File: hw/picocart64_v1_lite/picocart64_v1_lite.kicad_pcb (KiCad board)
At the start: 2 copper layers, 100 x 60 mm, 12 parts, among them J1 Conn_01x04, J2 Conn_01x07, J3 Conn_01x02, J4 Conn_01x01, J5 Conn_01x01, Q1 BSS84, U1 Pico, U4 N64-Cartridge

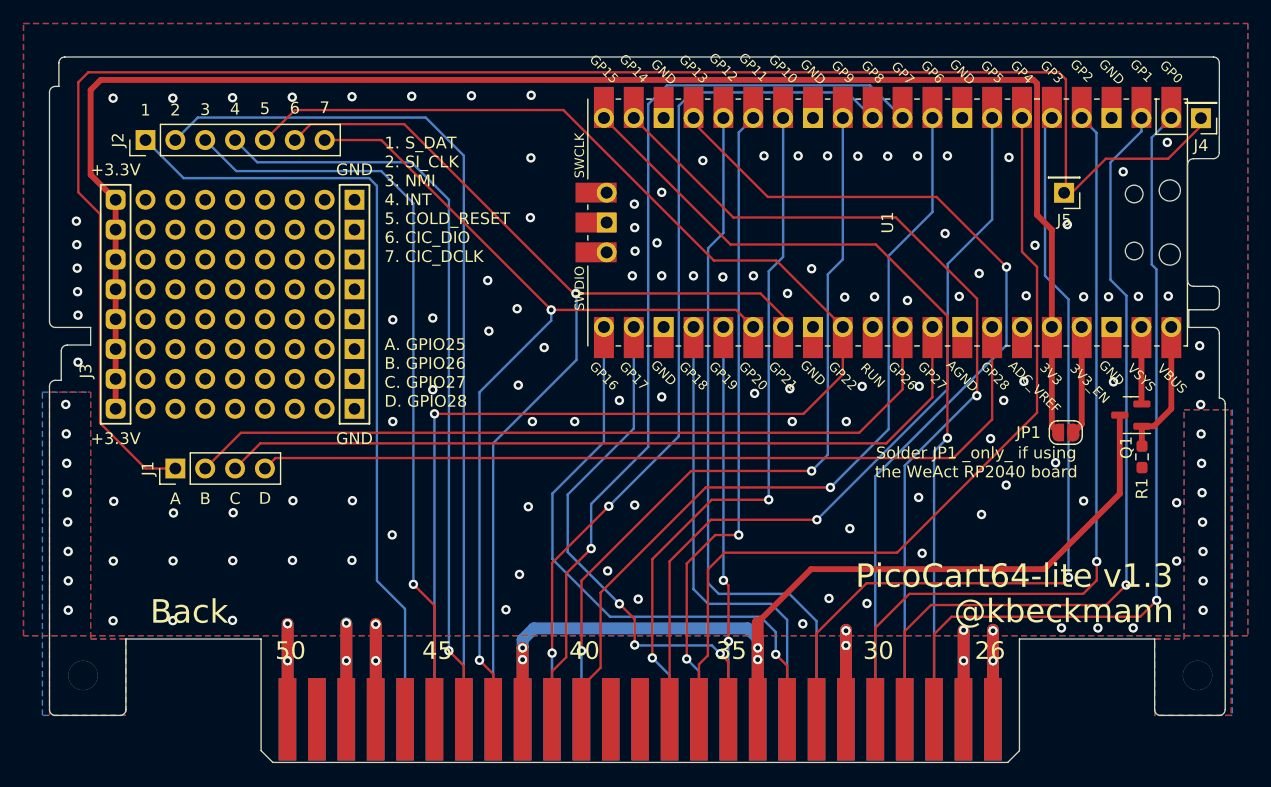
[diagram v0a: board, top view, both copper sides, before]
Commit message: Changes to v1 lite board to allow drop in weact as default instead of pico.
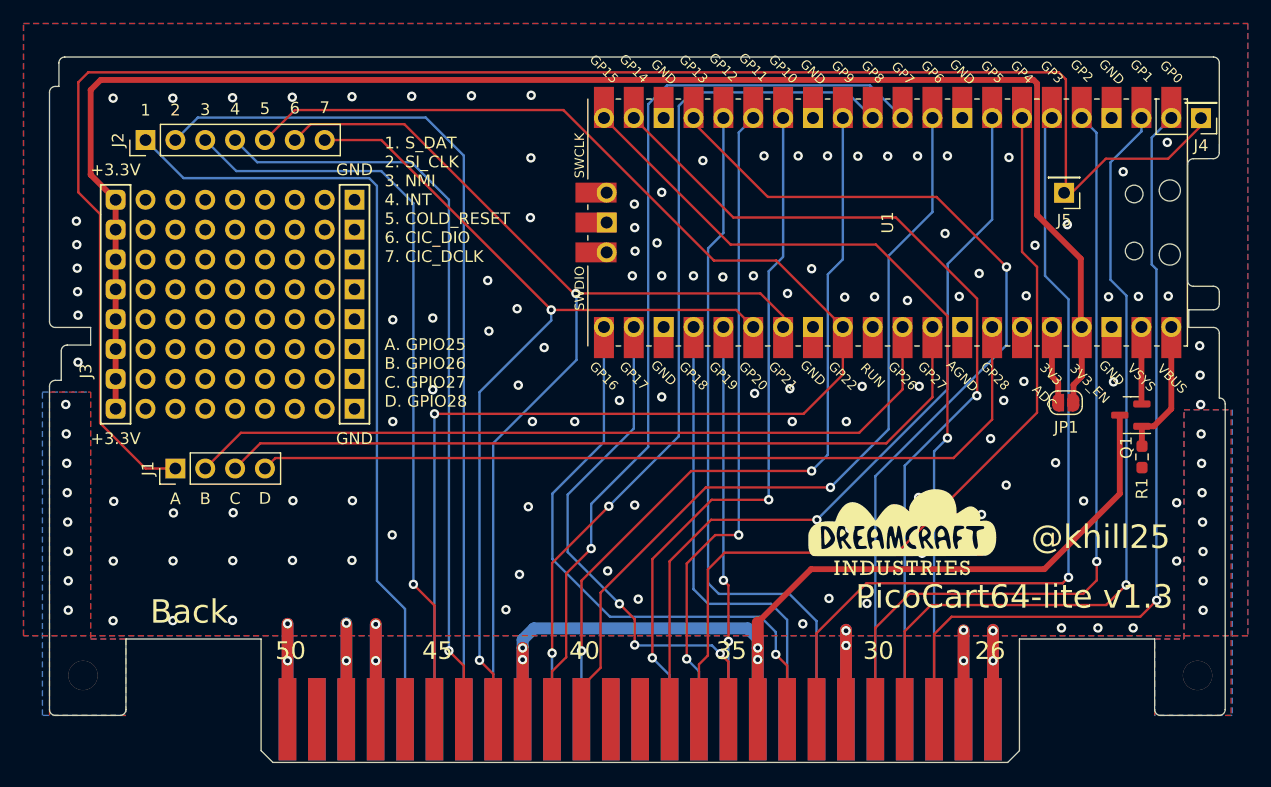
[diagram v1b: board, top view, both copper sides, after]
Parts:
- added G***: LOGO, LOGO, F.Cu at (172.5, 100.8)
- added G***: LOGO, LOGO, B.Cu at (181.4, 91.9)
- moved JP1 2.54 mm to (186.4, 89.4), turned to 0 degrees
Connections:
- JP1 pad 1: Net-(U1-Pad37) -> Net-(U1-Pad36)
- U1 pad 30: /~{RP_RESET} -> unconnected-(U1-Pad30)
- U1 pad 36: +3V3 -> Net-(U1-Pad36)
- U1 pad 37: Net-(U1-Pad37) -> +3V3
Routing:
- net Net-(U1-Pad37): track 9.27 -> 0.00 mm
- net Net-(U1-Pad36): track 0.00 -> 6.66 mm
- net +3V3: track 139.4 -> 138.0 mm
- net GND: vias 140 -> 139
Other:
- rule pad_to_mask_clearance: 0.13 -> 0
- board text removed: "Solder JP1 _only_ if using the WeAct RP2040 board"
